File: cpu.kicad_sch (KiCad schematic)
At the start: 30 parts, among them U2 Allwinner_V3S, Y1 24MHz, Y3 32.768kHz

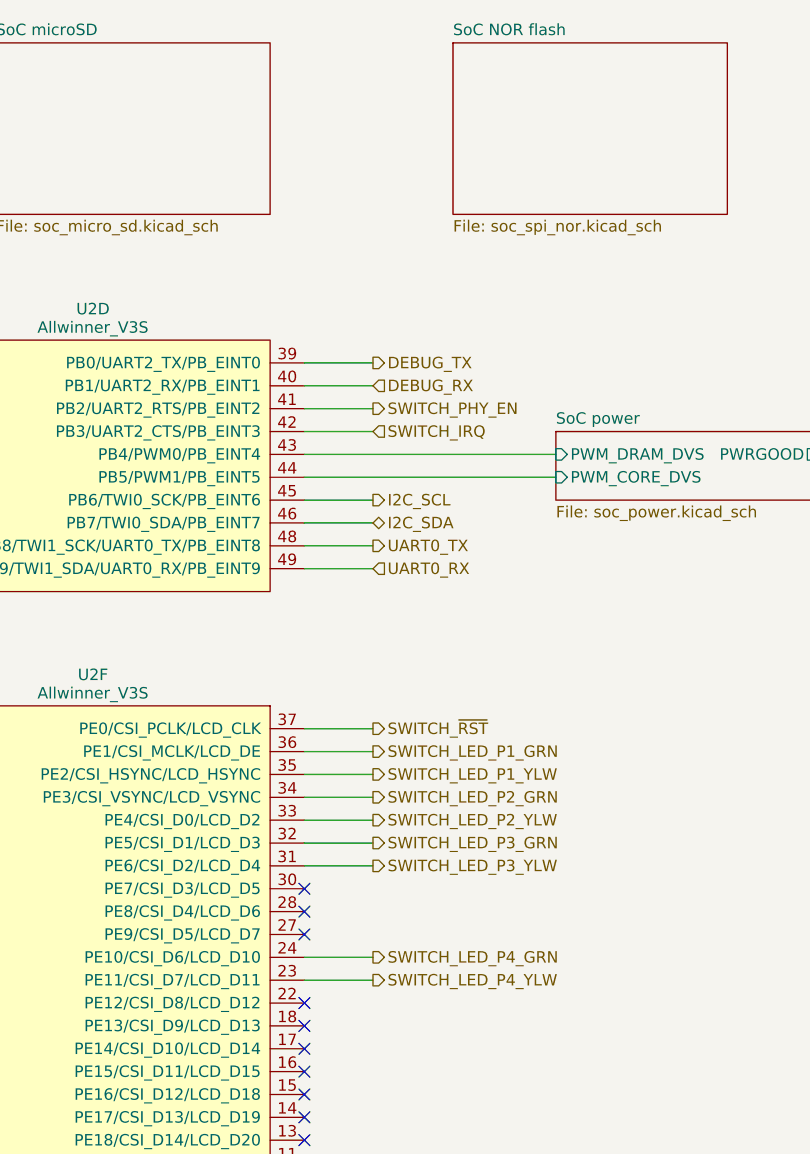
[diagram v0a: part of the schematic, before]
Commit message: Finish routing for the most part
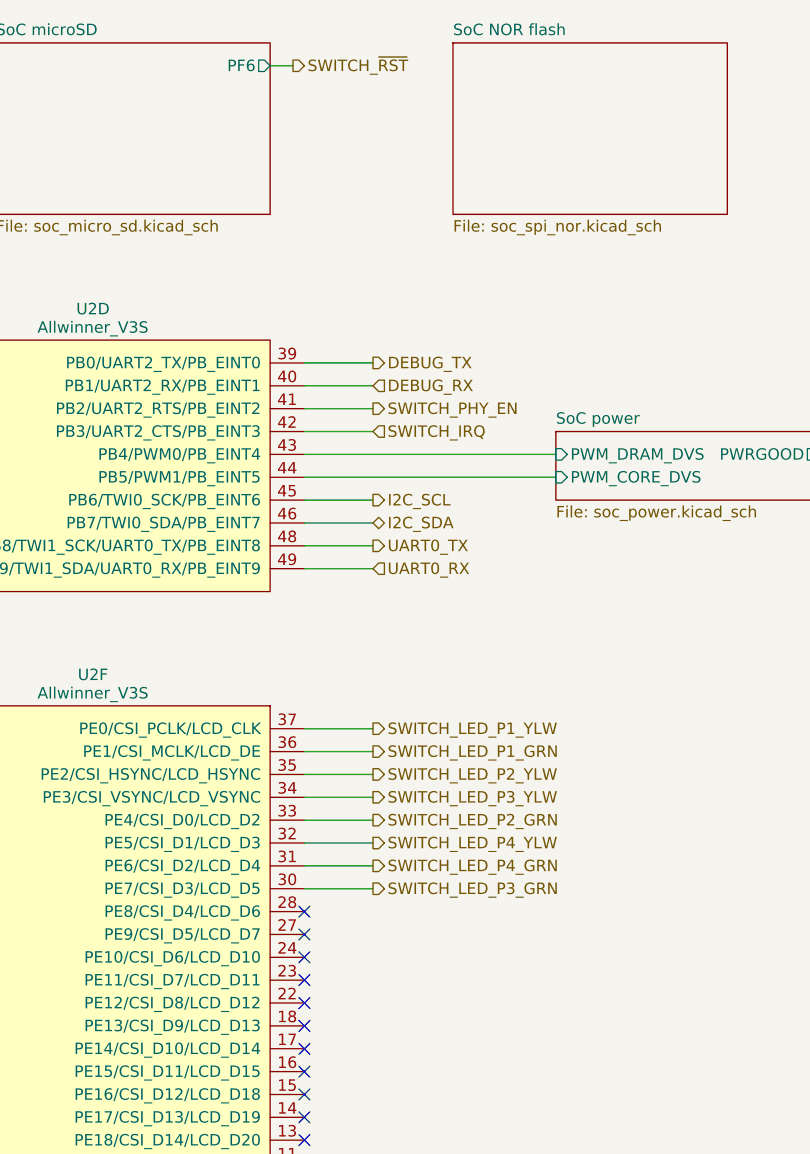
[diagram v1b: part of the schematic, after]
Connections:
- net SWITCH_LED_P1_YLW: now also U2.37 (PE0/CSI_PCLK/LCD_CLK); no longer U2.35 (PE2/CSI_HSYNC/LCD_HSYNC)
- net SWITCH_LED_P2_GRN: now also U2.33 (PE4/CSI_D0/LCD_D2); no longer U2.34 (PE3/CSI_VSYNC/LCD_VSYNC)
- net SWITCH_LED_P2_YLW: now also U2.35 (PE2/CSI_HSYNC/LCD_HSYNC); no longer U2.33 (PE4/CSI_D0/LCD_D2)
- net SWITCH_LED_P3_GRN: now also U2.30 (PE7/CSI_D3/LCD_D5); no longer U2.32 (PE5/CSI_D1/LCD_D3)
- net SWITCH_LED_P3_YLW: now also U2.34 (PE3/CSI_VSYNC/LCD_VSYNC); no longer U2.31 (PE6/CSI_D2/LCD_D4)
- net SWITCH_LED_P4_GRN: now also U2.31 (PE6/CSI_D2/LCD_D4); no longer U2.24 (PE10/CSI_D6/LCD_D10)
- net SWITCH_LED_P4_YLW: now also U2.32 (PE5/CSI_D1/LCD_D3); no longer U2.23 (PE11/CSI_D7/LCD_D11)
- net SWITCH_~{RST}: no longer U2.37 (PE0/CSI_PCLK/LCD_CLK)
- no-connect marks 15 -> 16
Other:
- sheet SoC microSD ports: added PF6; removed none

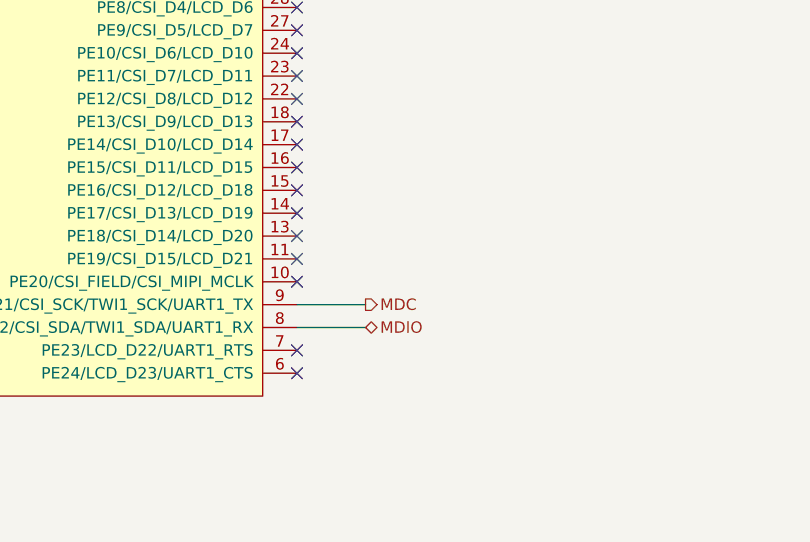
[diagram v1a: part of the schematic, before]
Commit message: Finalize design
- Layout last signals
- Hide designators
- Add more LEDs
- Add tooling holes
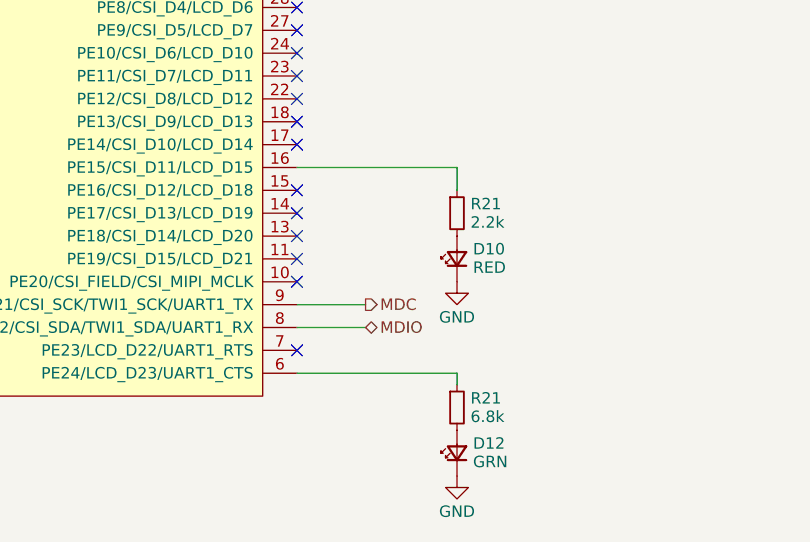
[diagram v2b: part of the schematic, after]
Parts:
- added D10: RED, LED_SMD:LED_0603_1608Metric, symbol Device:LED_Small
- added D12: GRN, LED_SMD:LED_0603_1608Metric, symbol Device:LED_Small
- added R21: 2.2k, Resistor_SMD:R_0402_1005Metric, symbol Device:R_Small
- added R21: 6.8k, Resistor_SMD:R_0402_1005Metric, symbol Device:R_Small
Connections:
- net GND: now also D10.1 (K), D12.1 (K)
- net at U2.16 (PE15/CSI_D11/LCD_D15): now also R21.1
- net at U2.6 (PE24/LCD_D23/UART1_CTS): now also R21.1
- new net: D10.2 (A), R21.2
- new net: D12.2 (A), R21.2
- no-connect marks 16 -> 14
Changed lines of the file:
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@@
   (no_connect (at 83.82 119.38))
   (no_connect (at 83.82 127))
-  (no_connect (at 83.82 129.54))
   (no_connect (at 83.82 134.62))
   (no_connect (at 83.82 121.92))
@@
   (no_connect (at 83.82 137.16))
   (no_connect (at 83.82 139.7))
-  (no_connect (at 83.82 152.4))
   (no_connect (at 83.82 124.46))
   (no_connect (at 83.82 116.84))
@@
     (stroke (width 0) (type default))
   )
+  (wire (pts (xy 101.6 129.54) (xy 101.6 132.08))
+    (stroke (width 0) (type default))
+  )
   (wire (pts (xy 245.11 132.08) (xy 245.11 133.35))
     (stroke (width 0) (type default))
@@
     (stroke (width 0) (type default))
   )
+  (wire (pts (xy 101.6 152.4) (xy 101.6 153.67))
+    (stroke (width 0) (type default))
+  )
   (wire (pts (xy 187.96 119.38) (xy 187.96 120.65))
     (stroke (width 0) (type default))
@@
     (stroke (width 0) (type default))
   )
+  (wire (pts (xy 83.82 129.54) (xy 101.6 129.54))
+    (stroke (width 0) (type default))
+  )
   (wire (pts (xy 33.02 48.26) (xy 33.02 50.8))
     (stroke (width 0) (type default))
@@
   )
   (wire (pts (xy 83.82 109.22) (xy 91.44 109.22))
+    (stroke (width 0) (type default))
+  )
+  (wire (pts (xy 83.82 152.4) (xy 101.6 152.4))
     (stroke (width 0) (type default))
   )
@@
     )
   )
+  (symbol (lib_id "Device:LED_Small") (at 101.6 139.7 90) (unit 1)
+    (in_bom yes) (on_board yes) (dnp no) (fields_autoplaced)
+    (property "Reference" "D10" (at 103.378 138.6125 90)
+      (effects (font (size 1.27 1.27)) (justify right))
+    )
+    (property "Value" "RED" (at 103.378 140.6605 90)
+      (effects (font (size 1.27 1.27)) (justify right))
+    )
+    (property "Footprint" "LED_SMD:LED_0603_1608Metric" (at 101.6 139.7 90)
+      (effects (font (size 1.27 1.27)) hide)
+    )
+    (property "Datasheet" "~" (at 101.6 139.7 90)
+      (effects (font (size 1.27 1.27)) hide)
+    )
+    (property "LCSC" "C2286" (at 101.6 139.7 90)
+      (effects (font (size 1.27 1.27)) hide)
+    )
+    (pin "1")
+    (pin "2")
+    (instances
+      (project "OpenHomeSwitch"
+        (path "/1d58c53f-167c-46c6-b61a-0c5d76c66e31/41bdf90a-7af2-4b3b-98f6-50835501a67f"
+          (reference "D10") (unit 1)
+        )
+        (path "/1d58c53f-167c-46c6-b61a-0c5d76c66e31"
+          (reference "D7") (unit 1)
+        )
+      )
+    )
+  )
   (symbol (lib_id "power:GND") (at 27.94 101.6 0) (unit 1)
     (in_bom yes) (on_board yes) (dnp no) (fields_autoplaced)
@@
         (path "/1d58c53f-167c-46c6-b61a-0c5d76c66e31/41bdf90a-7af2-4b3b-98f6-50835501a67f"
           (reference "C118") (unit 1)
+        )
+      )
+    )
+  )
+  (symbol (lib_id "power:GND") (at 101.6 163.83 0) (unit 1)
+    (in_bom yes) (on_board yes) (dnp no) (fields_autoplaced)
+    (property "Reference" "#PWR0169" (at 101.6 170.18 0)
+      (effects (font (size 1.27 1.27)) hide)
+    )
+    (property "Value" "GND" (at 101.6 167.775 0)
+      (effects (font (size 1.27 1.27)))
+    )
+    (property "Footprint" "" (at 101.6 163.83 0)
+      (effects (font (size 1.27 1.27)) hide)
+    )
+    (property "Datasheet" "" (at 101.6 163.83 0)
+      (effects (font (size 1.27 1.27)) hide)
+    )
+    (pin "1")
+    (instances
+      (project "OpenHomeSwitch"
+        (path "/1d58c53f-167c-46c6-b61a-0c5d76c66e31"
+          (reference "#PWR0169") (unit 1)
+        )
+        (path "/1d58c53f-167c-46c6-b61a-0c5d76c66e31/41bdf90a-7af2-4b3b-98f6-50835501a67f"
+          (reference "#PWR0175") (unit 1)
+        )
+      )
+    )
+  )
+  (symbol (lib_id "power:GND") (at 101.6 142.24 0) (unit 1)
+    (in_bom yes) (on_board yes) (dnp no) (fields_autoplaced)
+    (property "Reference" "#PWR0146" (at 101.6 148.59 0)
+      (effects (font (size 1.27 1.27)) hide)
+    )
+    (property "Value" "GND" (at 101.6 146.185 0)
+      (effects (font (size 1.27 1.27)))
+    )
+    (property "Footprint" "" (at 101.6 142.24 0)
+      (effects (font (size 1.27 1.27)) hide)
+    )
+    (property "Datasheet" "" (at 101.6 142.24 0)
+      (effects (font (size 1.27 1.27)) hide)
+    )
+    (pin "1")
+    (instances
+      (project "OpenHomeSwitch"
+        (path "/1d58c53f-167c-46c6-b61a-0c5d76c66e31"
+          (reference "#PWR0146") (unit 1)
+        )
+        (path "/1d58c53f-167c-46c6-b61a-0c5d76c66e31/41bdf90a-7af2-4b3b-98f6-50835501a67f"
+          (reference "#PWR0171") (unit 1)
         )
       )
@@
     )
   )
+  (symbol (lib_id "Device:R_Small") (at 101.6 134.62 0) (unit 1)
+    (in_bom yes) (on_board yes) (dnp no)
+    (property "Reference" "R21" (at 103.0986 133.596 0)
+      (effects (font (size 1.27 1.27)) (justify left))
+    )
+    (property "Value" "2.2k" (at 103.0986 135.644 0)
+      (effects (font (size 1.27 1.27)) (justify left))
+    )
+    (property "Footprint" "Resistor_SMD:R_0402_1005Metric" (at 101.6 134.62 0)
+      (effects (font (size 1.27 1.27)) hide)
+    )
+    (property "Datasheet" "~" (at 101.6 134.62 0)
+      (effects (font (size 1.27 1.27)) hide)
+    )
+    (property "LCSC" "C25879" (at 101.6 134.62 0)
+      (effects (font (size 1.27 1.27)) hide)
+    )
+    (pin "1")
+    (pin "2")
+    (instances
+      (project "OpenHomeSwitch"
+        (path "/1d58c53f-167c-46c6-b61a-0c5d76c66e31/063037d5-ac42-4d44-866d-25c29bbefbbd"
+          (reference "R21") (unit 1)
+        )
+        (path "/1d58c53f-167c-46c6-b61a-0c5d76c66e31/41bdf90a-7af2-4b3b-98f6-50835501a67f/979e57af-5604-4f99-9831-27ac90839e99"
+          (reference "R26") (unit 1)
+        )
+        (path "/1d58c53f-167c-46c6-b61a-0c5d76c66e31/41bdf90a-7af2-4b3b-98f6-50835501a67f"
+          (reference "R75") (unit 1)
+        )
+      )
+    )
+  )
   (symbol (lib_id "Device:C_Small") (at 33.02 97.79 180) (unit 1)
     (in_bom yes) (on_board yes) (dnp no)
@@
         (path "/1d58c53f-167c-46c6-b61a-0c5d76c66e31/41bdf90a-7af2-4b3b-98f6-50835501a67f"
           (reference "#PWR0105") (unit 1)
+        )
+      )
+    )
+  )
+  (symbol (lib_id "Device:LED_Small") (at 101.6 161.29 90) (unit 1)
+    (in_bom yes) (on_board yes) (dnp no) (fields_autoplaced)
+    (property "Reference" "D12" (at 103.378 160.2025 90)
+      (effects (font (size 1.27 1.27)) (justify right))
+    )
+    (property "Value" "GRN" (at 103.378 162.2505 90)
+      (effects (font (size 1.27 1.27)) (justify right))
+    )
+    (property "Footprint" "LED_SMD:LED_0603_1608Metric" (at 101.6 161.29 90)
+      (effects (font (size 1.27 1.27)) hide)
+    )
+    (property "Datasheet" "~" (at 101.6 161.29 90)
+      (effects (font (size 1.27 1.27)) hide)
+    )
+    (property "LCSC" "C72043" (at 101.6 161.29 90)
+      (effects (font (size 1.27 1.27)) hide)
+    )
+    (pin "1")
+    (pin "2")
+    (instances
+      (project "OpenHomeSwitch"
+        (path "/1d58c53f-167c-46c6-b61a-0c5d76c66e31/41bdf90a-7af2-4b3b-98f6-50835501a67f"
+          (reference "D12") (unit 1)
+        )
+        (path "/1d58c53f-167c-46c6-b61a-0c5d76c66e31"
+          (reference "D9") (unit 1)
         )
       )
@@
         )
       )
+    )
+  )
+  (symbol (lib_id "Device:R_Small") (at 101.6 156.21 0) (unit 1)
+    (in_bom yes) (on_board yes) (dnp no)
+    (property "Reference" "R21" (at 103.0986 155.186 0)
+      (effects (font (size 1.27 1.27)) (justify left))
+    )
+    (property "Value" "6.8k" (at 103.0986 157.234 0)
+      (effects (font (size 1.27 1.27)) (justify left))
+    )
+    (property "Footprint" "Resistor_SMD:R_0402_1005Metric" (at 101.6 156.21 0)
+      (effects (font (size 1.27 1.27)) hide)
+    )
+    (property "Datasheet" "~" (at 101.6 156.21 0)
+      (effects (font (size 1.27 1.27)) hide)
+    )
+    (property "LCSC" "C25917" (at 101.6 156.21 0)
+      (effects (font (size 1.27 1.27)) hide)
+    )
+    (pin "1")
+    (pin "2")
+    (instances
+      (project "OpenHomeSwitch"
+        (path "/1d58c53f-167c-46c6-b61a-0c5d76c66e31/063037d5-ac42-4d44-866d-25c29bbefbbd"
+          (reference "R21") (unit 1)
+        )
+        (path "/1d58c53f-167c-46c6-b61a-0c5d76c66e31/41bdf90a-7af2-4b3b-98f6-50835501a67f/979e57af-5604-4f99-9831-27ac90839e99"
+          (reference "R26") (unit 1)
+        )
+        (path "/1d58c53f-167c-46c6-b61a-0c5d76c66e31/41bdf90a-7af2-4b3b-98f6-50835501a67f"
+          (reference "R85") (unit 1)
+        )
+        (path "/1d58c53f-167c-46c6-b61a-0c5d76c66e31"
+          (reference "R51") (unit 1)
+        )
+      )

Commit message: Add V3s variant with smaller exposed GND pad
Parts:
- U2: footprint Package_QFP_Allwinner:LQFP-128_14x14mm_P0.4mm_EPAD_8x8mm -> Package_QFP_Allwinner:LQFP-128_14x14mm_P0.4mm_EPAD_5.72x5.72mm
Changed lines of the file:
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@@
       (effects (font (size 1.27 1.27)))
     )
-    (property "Footprint" "Package_QFP_Allwinner:LQFP-128_14x14mm_P0.4mm_EPAD_8x8mm" (at 88.9 119.38 0)
+    (property "Footprint" "Package_QFP_Allwinner:LQFP-128_14x14mm_P0.4mm_EPAD_5.72x5.72mm" (at 88.9 119.38 0)
       (effects (font (size 1.27 1.27)) hide)
     )
@@
       (effects (font (size 1.27 1.27)))
     )
-    (property "Footprint" "Package_QFP_Allwinner:LQFP-128_14x14mm_P0.4mm_EPAD_8x8mm" (at 237.49 138.43 0)
+    (property "Footprint" "Package_QFP_Allwinner:LQFP-128_14x14mm_P0.4mm_EPAD_5.72x5.72mm" (at 237.49 138.43 0)
       (effects (font (size 1.27 1.27)) hide)
     )
@@
       (effects (font (size 1.27 1.27)))
     )
-    (property "Footprint" "Package_QFP_Allwinner:LQFP-128_14x14mm_P0.4mm_EPAD_8x8mm" (at 88.9 78.74 0)
+    (property "Footprint" "Package_QFP_Allwinner:LQFP-128_14x14mm_P0.4mm_EPAD_5.72x5.72mm" (at 88.9 78.74 0)
       (effects (font (size 1.27 1.27)) hide)
     )
@@
       (effects (font (size 1.27 1.27)))
     )
-    (property "Footprint" "Package_QFP_Allwinner:LQFP-128_14x14mm_P0.4mm_EPAD_8x8mm" (at 234.95 59.69 0)
-      (effects (font (size 1.27 1.27)) hide)
-    )
+    (property "Footprint" "Package_QFP_Allwinner:LQFP-128_14x14mm_P0.4mm_EPAD_5.72x5.72mm" (at 234.95 59.69 0)
+      (effects (font (size 1.27 1.27)) hide)
+    )

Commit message: Fix LCSC part numbers
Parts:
- U2: LCSC (none) -> C2687449
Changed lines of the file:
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@@
+      (effects (font (size 1.27 1.27)) hide)
+    )
+    (property "LCSC" "C2687449" (at 60.96 88.9 0)
       (effects (font (size 1.27 1.27)) hide)
     )
@@
       (effects (font (size 1.27 1.27)) hide)
     )
+    (property "LCSC" "C2687449" (at 209.55 107.95 0)
+      (effects (font (size 1.27 1.27)) hide)
+    )
     (pin "110")
     (pin "111")
@@
       (effects (font (size 1.27 1.27)) hide)
     )
+    (property "LCSC" "C2687449" (at 60.96 48.26 0)
+      (effects (font (size 1.27 1.27)) hide)
+    )
     (pin "110")
     (pin "111")
@@
       (effects (font (size 1.27 1.27)) hide)
     )
+    (property "LCSC" "C2687449" (at 207.01 29.21 0)
+      (effects (font (size 1.27 1.27)) hide)
+    )

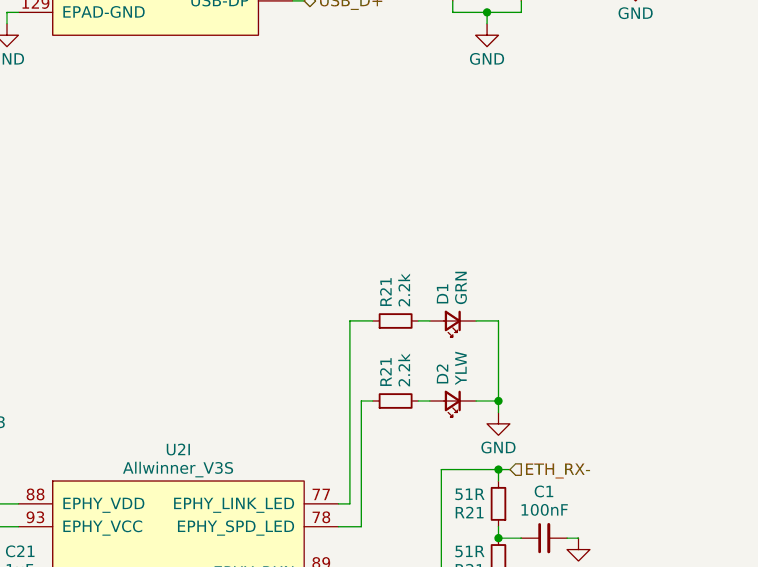
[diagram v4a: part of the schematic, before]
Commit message: Replace 2.2k LED current limiting resistor by 10k one
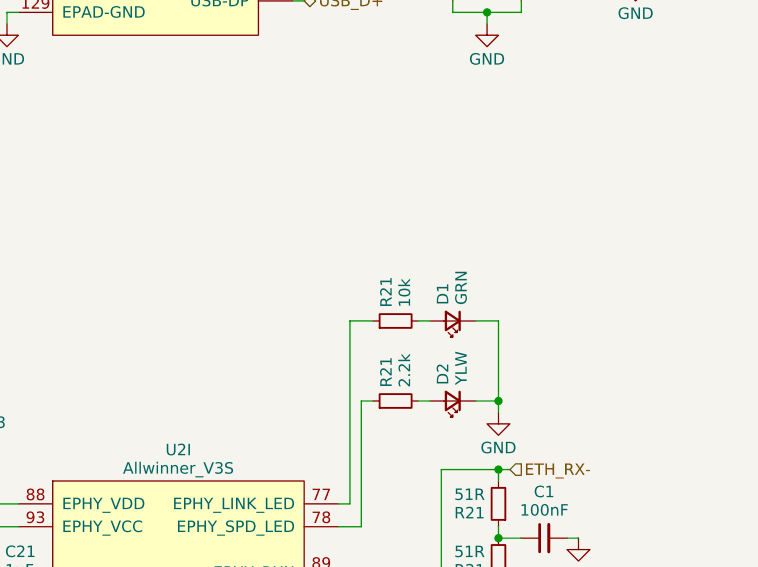
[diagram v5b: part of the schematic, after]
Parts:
- R21: value 2.2k -> 10k; LCSC C25879 -> C25744
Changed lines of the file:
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@@
       (effects (font (size 1.27 1.27)) (justify left))
     )
-    (property "Value" "2.2k" (at 234.704 88.6714 0)
+    (property "Value" "10k" (at 234.704 88.6714 0)
       (effects (font (size 1.27 1.27)) (justify left))
     )
@@
       (effects (font (size 1.27 1.27)) hide)
     )
-    (property "LCSC" "C25879" (at 233.68 90.17 0)
+    (property "LCSC" "C25744" (at 233.68 90.17 0)
       (effects (font (size 1.27 1.27)) hide)
     )
